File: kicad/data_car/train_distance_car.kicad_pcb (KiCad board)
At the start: 2 copper layers, 120.7 x 50.8 mm, 28 parts, among them J1 Encoder Header, J2 Button Header, J3 IFI9431 Header, J4 Button Header, J5 Adafruit 500C Header, U1 Teensy3.2, U2 MB85RS16

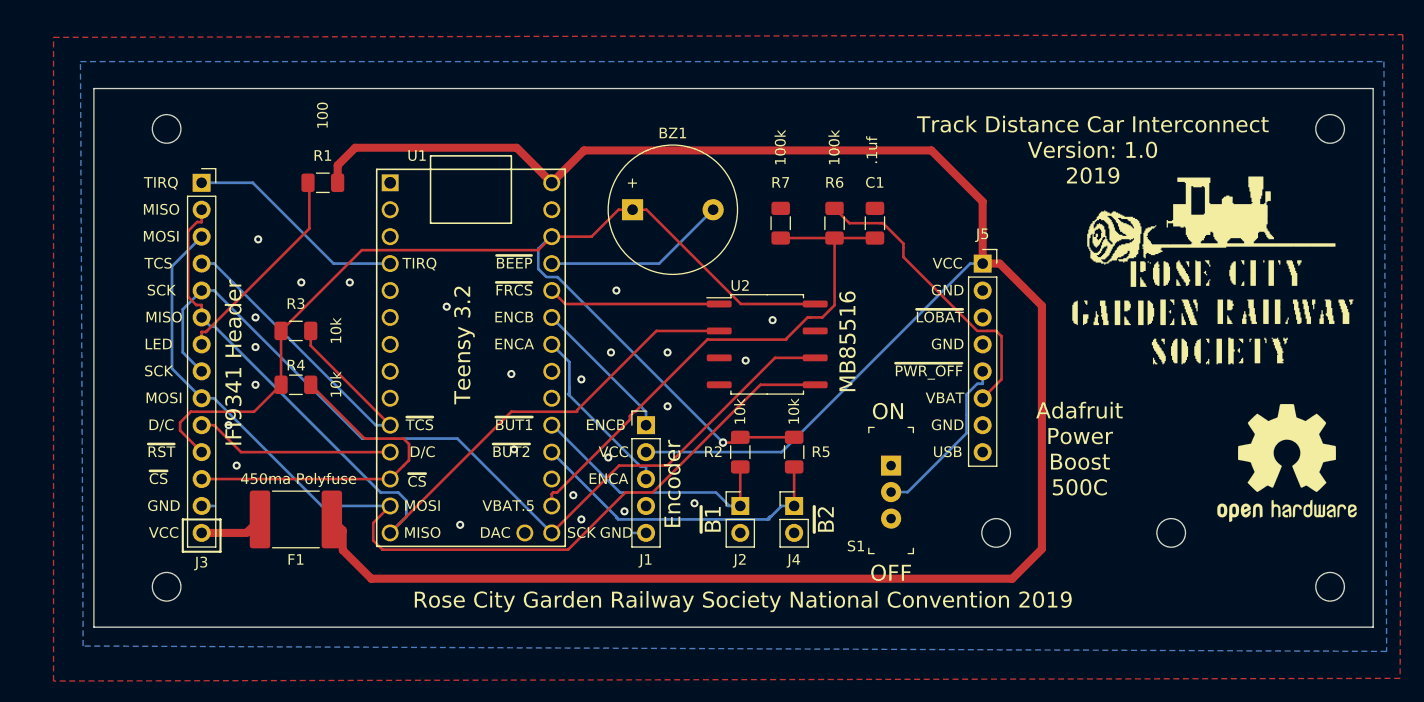
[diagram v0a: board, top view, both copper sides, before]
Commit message: Update to version 1.2 PCB - fixed parts profiles.  Changes to be committed: 	deleted:    kicad/data_car/sym-lib-table 	deleted:    kicad/data_car/train_distance_car-cache.lib 	deleted:    kicad/data_car/train_distance_car.bak 	deleted:    kicad/data_car/train_distance_car.dsn 	modified:   kicad/data_car/train_distance_car.kicad_pcb 	deleted:    kicad/data_car/train_distance_car.kicad_pcb-bak 	deleted:    kicad/data_car/train_distance_car.net 	deleted:    kicad/data_car/train_distance_car.pro 	deleted:    kicad/data_car/train_distance_car.rules 	modified:   kicad/data_car/train_distance_car.sch 	deleted:    kicad/data_car/train_distance_car.ses 	deleted:    kicad/data_car/train_distance_car_v1.kicad_pcb
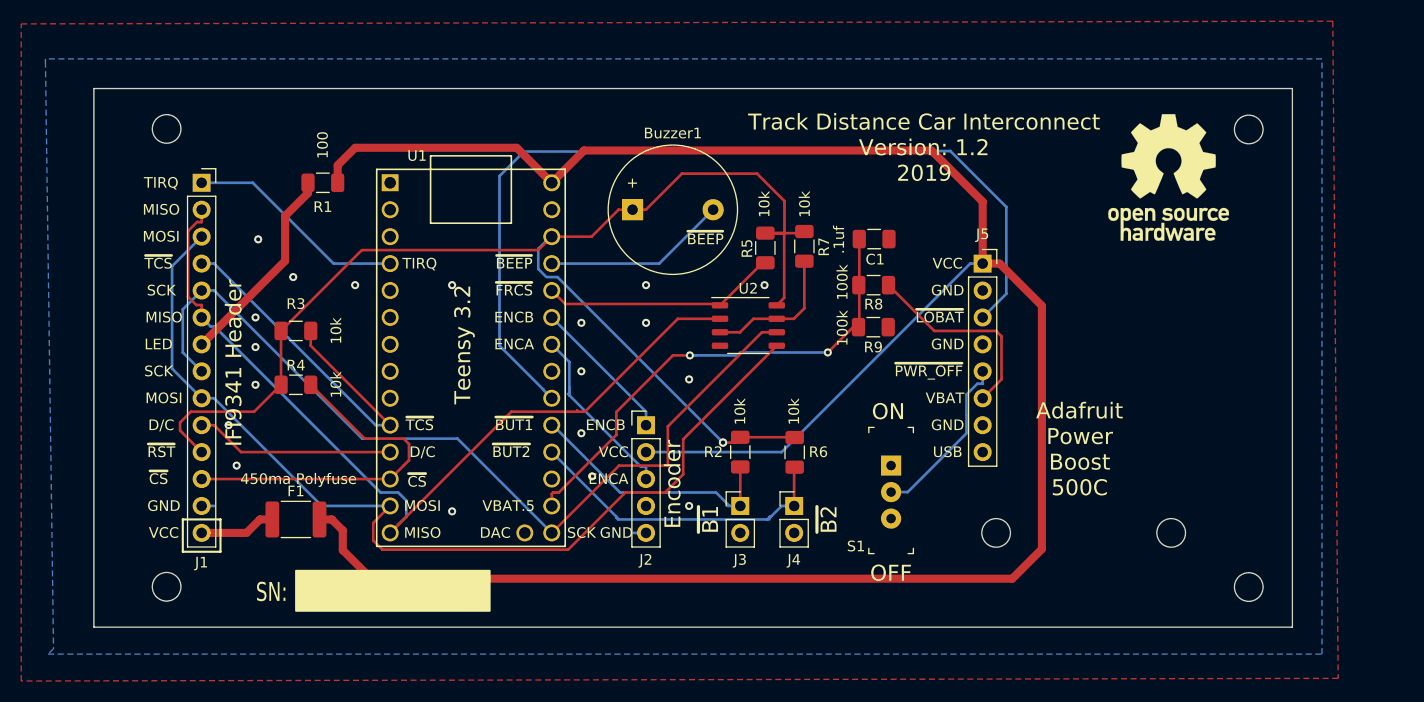
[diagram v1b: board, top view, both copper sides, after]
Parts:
- removed the RCGRS_sm at (148.3, 70.1)
- removed the RCGRS_sm at (173.7, 77.2)
- removed the REF** at (125.7, 71.9)
- removed the REF** at (169.7, 98.8)
- added R8: 100k, Resistor_SMD:R_1206_3216Metric, F.Cu at (130.7, 82.0)
- added R9: 100k, Resistor_SMD:R_1206_3216Metric, F.Cu at (130.7, 86.0)
- added RCGRS_sm: , teensy:RCGRS_sm, B.Cu at (109.5, 98.3)
- added REF**: OSHW-Logo_11.4x12mm_SilkScreen, Symbol:OSHW-Logo_11.4x12mm_SilkScreen, B.Cu at (155.7, 87.9)
- added REF**: OSHW-Logo_11.4x12mm_SilkScreen, Symbol:OSHW-Logo_11.4x12mm_SilkScreen, F.Cu at (158.5, 71.9)
- F1: footprint Fuse:Fuse_2920_7451Metric -> Fuse:Fuse_1812_4532Metric_Pad1.30x3.40mm_HandSolder
- R6, R7: value 100k -> 10k
- U2: footprint Package_SO:SOP-8_6.62x9.15mm_P2.54mm -> Package_SO:SSOP-8_3.9x5.05mm_P1.27mm
- moved R6 21.9 mm to (123.2, 97.8)
- moved R5 19.4 mm to (120.5, 78.5)
- moved H5 7.67 mm to (166.1, 67.4)
- moved H6 7.67 mm to (166.1, 110.5)
- moved R7 3.13 mm to (124.2, 78.4), turned to 270 degrees
- moved U2 2.51 mm to (118.9, 85.9)
- moved C1 1.50 mm to (130.7, 77.7), turned to 0 degrees
- renumbered BZ1 to Buzzer1, J3 to J1, J1 to J2, J2 to J3
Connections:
- net CS renamed ~CS
- net TCS renamed ~TCS
- J2 pad 4: Net-(J1-Pad4) -> (no net)
- J5 pad 8: Net-(J5-Pad8) -> (no net)
- R5 pad 2: ~BUTTON2 -> ~FRCS
- R6 pad 1: VBAT -> +3V3
- R6 pad 2: VBAT.5 -> ~BUTTON2
- R7 pad 1: VBAT.5 -> +3V3
- R7 pad 2: GND -> Net-(R7-Pad2)
- S1 pad 1: Net-(S1-Pad1) -> (no net)
- U1 pad 19: Net-(U1-Pad19) -> (no net)
- U1 pad 2: Net-(U1-Pad2) -> (no net)
- U1 pad 22: Net-(U1-Pad22) -> (no net)
- U1 pad 25: Net-(U1-Pad25) -> ~LOBAT
- U1 pad 26: Net-(U1-Pad26) -> (no net)
- U1 pad 3: Net-(U1-Pad3) -> (no net)
- U1 pad 5: Net-(U1-Pad5) -> (no net)
- U1 pad 6: Net-(U1-Pad6) -> (no net)
- U1 pad 7: Net-(U1-Pad7) -> (no net)
- U1 pad 8: Net-(U1-Pad8) -> (no net)
- U1 pad 9: Net-(U1-Pad9) -> (no net)
- U2 pad 3: Net-(U2-Pad3) -> Net-(R7-Pad2)
- U2 pad 7: Net-(U2-Pad7) -> Net-(R7-Pad2)
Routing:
- net ~LOBAT: track 0.00 -> 85.3 mm
- net Net-(R7-Pad2): track 0.00 -> 13.3 mm
- net +3V3: track 113.0 -> 124.5 mm
- net VBAT: track 28.0 -> 19.2 mm
- net ~FRCS: track 16.3 -> 22.3 mm
- net VBAT.5: track 50.8 -> 46.3 mm, vias 0 -> 2
- net +5V: track 214.5 -> 215.6 mm
- net Net-(F1-Pad1): track 6.03 -> 7.19 mm
- net MISO: track 80.8 -> 81.4 mm
- net GND: vias 24 -> 19
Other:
- board size 120.7 x 50.8 mm -> 113 x 50.8 mm
- board text added: "SN:"
- board text added: "Track Distance Car Interconnect Version: 1.2 2019"
- board text added: "Track Distance Car Interconnect Version: 1.2 Eric Timberlake - 2019"
- board text removed: "MB85516"
- board text removed: "Rose City Garden Railway Society National Convention 2019"
- board text removed: "TCS"
- board text removed: "Track Distance Car Interconnect Version: 1.0 2019"
- board text removed: "Track Distance Car Interconnect Version: 1.0 Eric Timberlake - 2019"
